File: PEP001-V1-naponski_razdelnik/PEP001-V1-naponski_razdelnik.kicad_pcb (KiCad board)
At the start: 2 copper layers, 45 x 45 mm, 11 parts, among them J1 Screw_Terminal_01x02

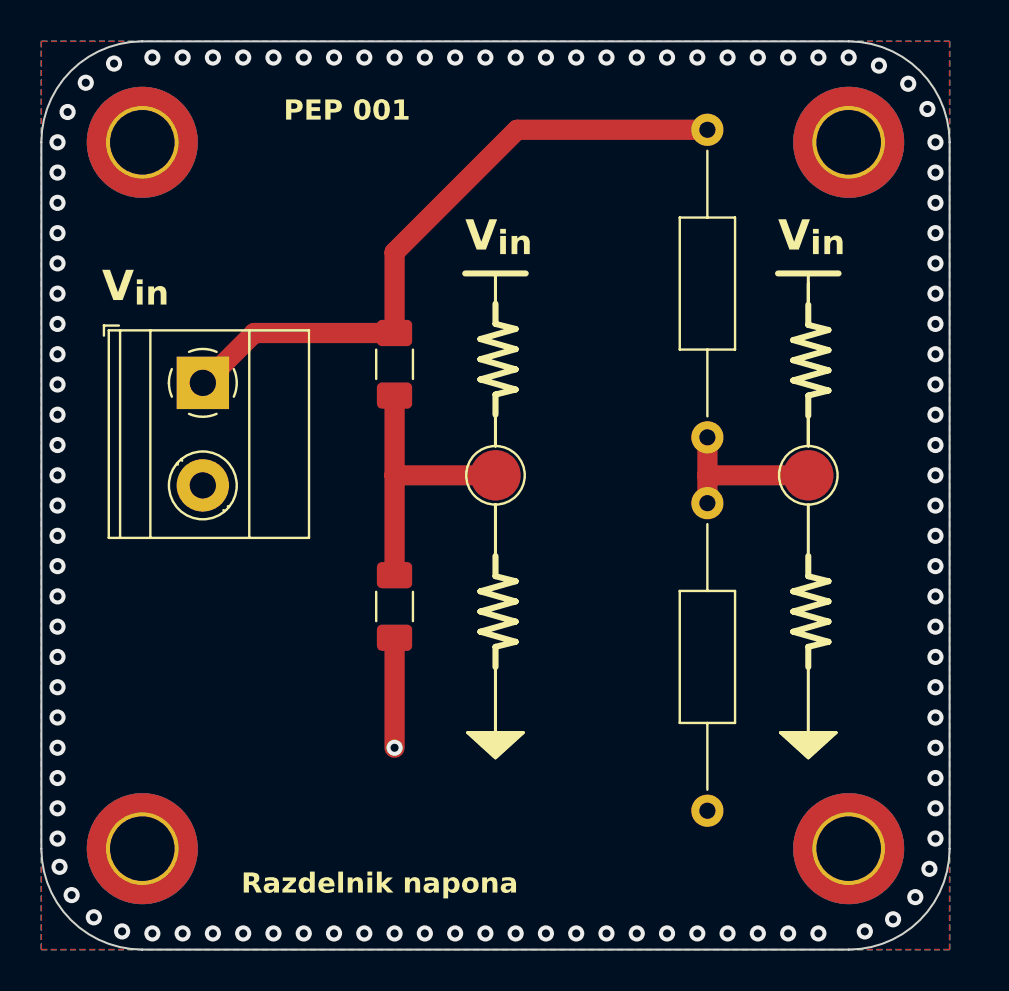
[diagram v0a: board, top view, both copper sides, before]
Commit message: PEP001 - Only LCSL linking left.
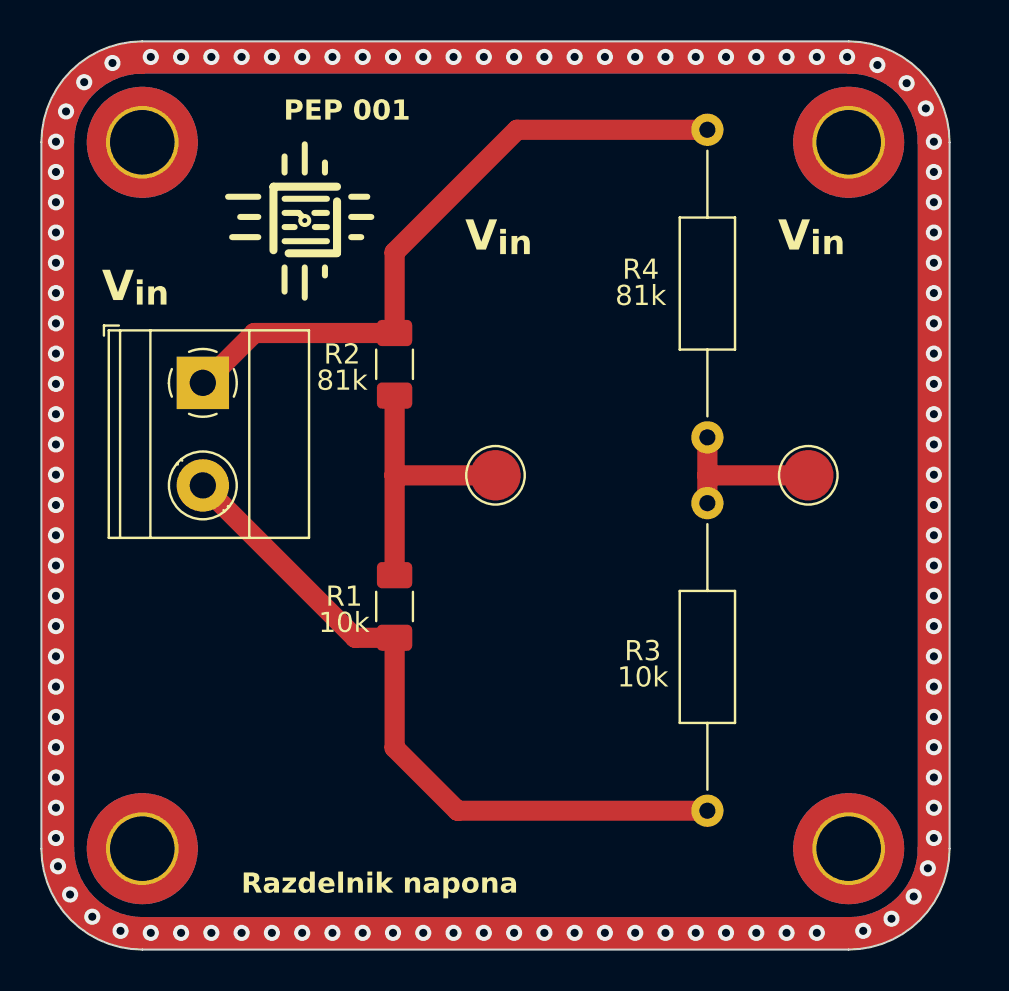
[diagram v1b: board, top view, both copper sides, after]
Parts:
- added REF**: ele_petnica_logo, PEP_library:ele_petnica_logo, F.Cu at (117.0, 69.9)
- R2, R4: value 90k -> 81k
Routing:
- net 0: track 5.45 -> 34.9 mm, vias 110 -> 0
- net (no net): vias 0 -> 109
- removed copper zone on B.Cu, net 0
- removed copper zone on F.Cu, net 0
